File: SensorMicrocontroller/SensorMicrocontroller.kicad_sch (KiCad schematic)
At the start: 35 parts, among them J1 JST B6B-PH-SM4-TB, J10 12V Connector, J11 Light Connector, J2 JST B4B-PH-SM4-TB, J3 JST B4B-PH-SM4-TB, J4 JST B4B-PH-SM4-TB, J5 JST B4B-PH-SM4-TB, J6 Fan0, J7 Fan1, J8 Fan2, J9 Fan3, Q1 DMT6009LCT, Q2 DMT6009LCT, U1 SC0915, U2 ADS1115IDGS

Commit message: Added manufacturer part number to parts
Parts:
- C1: Manufacturer Part Number (none) -> CC0805KRX7R9BB104
- F1: Manufacturer Part Number (none) -> MFU0805FF01000P500
- J1: Manufacturer Part Number (none) -> B6B-PH-SM4-TB
- J10: Manufacturer Part Number (none) -> B2B-PH-SM4-TB
- J11: Manufacturer Part Number (none) -> B4B-EH-A
- J2, J3, J4, J5: Manufacturer Part Number (none) -> B4B-PH-SM4-TB
- J6: value Fan0 -> ~; Manufacturer Part Number (none) -> 0470531000
- J7: value Fan1 -> ~; Manufacturer Part Number (none) -> 0470531000
- J8: value Fan2 -> ~; Manufacturer Part Number (none) -> 0470531000
- J9: value Fan3 -> ~; Manufacturer Part Number (none) -> 0470531000
- Q1, Q2: Manufacturer Part Number (none) -> DMT6009LCT
- R1, R2: Manufacturer Part Number (none) -> CRCW08054K70FKEAC
- R10, R11, R12, R7, R8, R9: value 175 -> 174; Manufacturer Part Number (none) -> RC0805FR-07174RL
- R3, R4, R5, R6: Manufacturer Part Number (none) -> RR1220P-103-D
- U1: value SC0915 -> Pico; Manufacturer Part Number (none) -> SC0915
- U2: Manufacturer Part Number (none) -> ADS1115IDGSR
- U4, U5, U6, U7, U8, U9: value ~ -> Optoisolators; Manufacturer Part Number (none) -> TLP2355(TPL,E
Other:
- note added: "Fan0"
- note added: "Fan1"
- note added: "Fan2"
- note added: "Fan3"

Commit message: Updated date and revision number
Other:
- note added: "1.4"
- note added: "1/27/25"
- note removed: "1.3"
- note removed: "1/9/25"

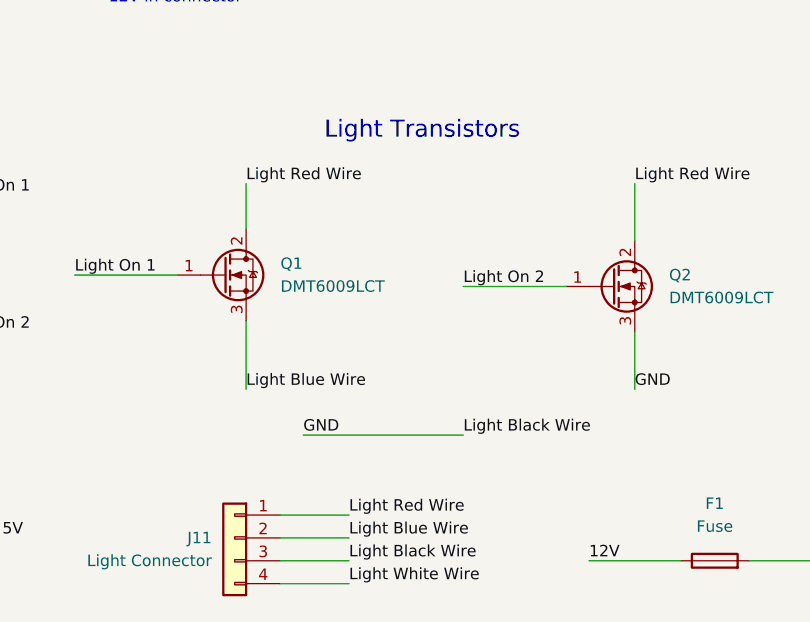
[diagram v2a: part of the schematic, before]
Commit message: Updated transistor wiring diagram
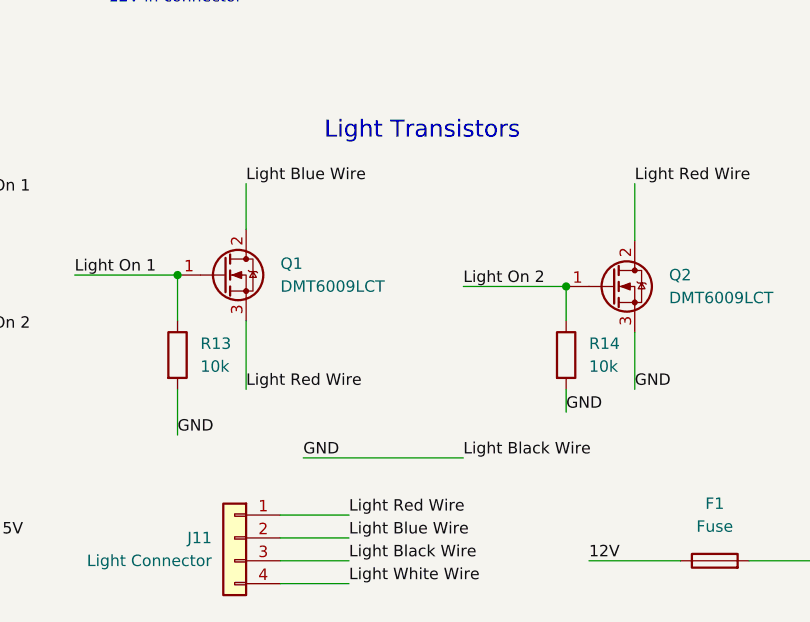
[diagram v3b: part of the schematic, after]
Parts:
- added R13, R14: 10k, Resistor_SMD:R_0805_2012Metric, symbol Device:R
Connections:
- net GND: now also R13.2, R14.2
- net Light Blue Wire: now also Q1.2 (D); no longer Q1.3 (S)
- net Light On 1: now also R13.1
- net Light On 2: now also R14.1
- net Light Red Wire: now also Q1.3 (S); no longer Q1.2 (D)

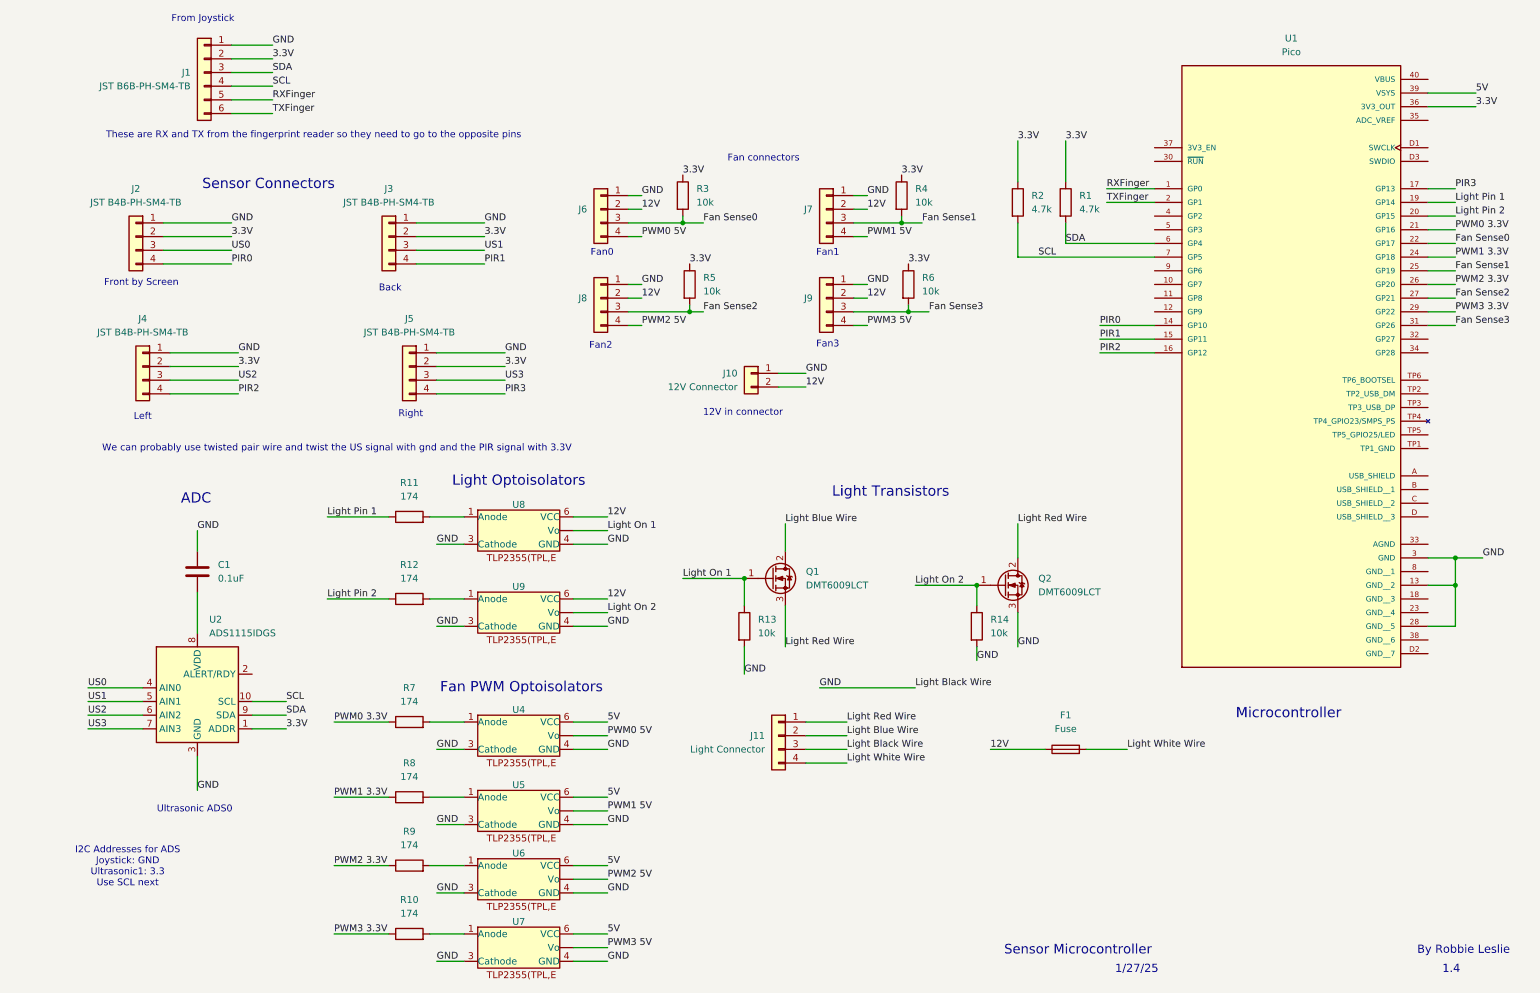
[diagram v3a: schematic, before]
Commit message: Worked on PCB layout
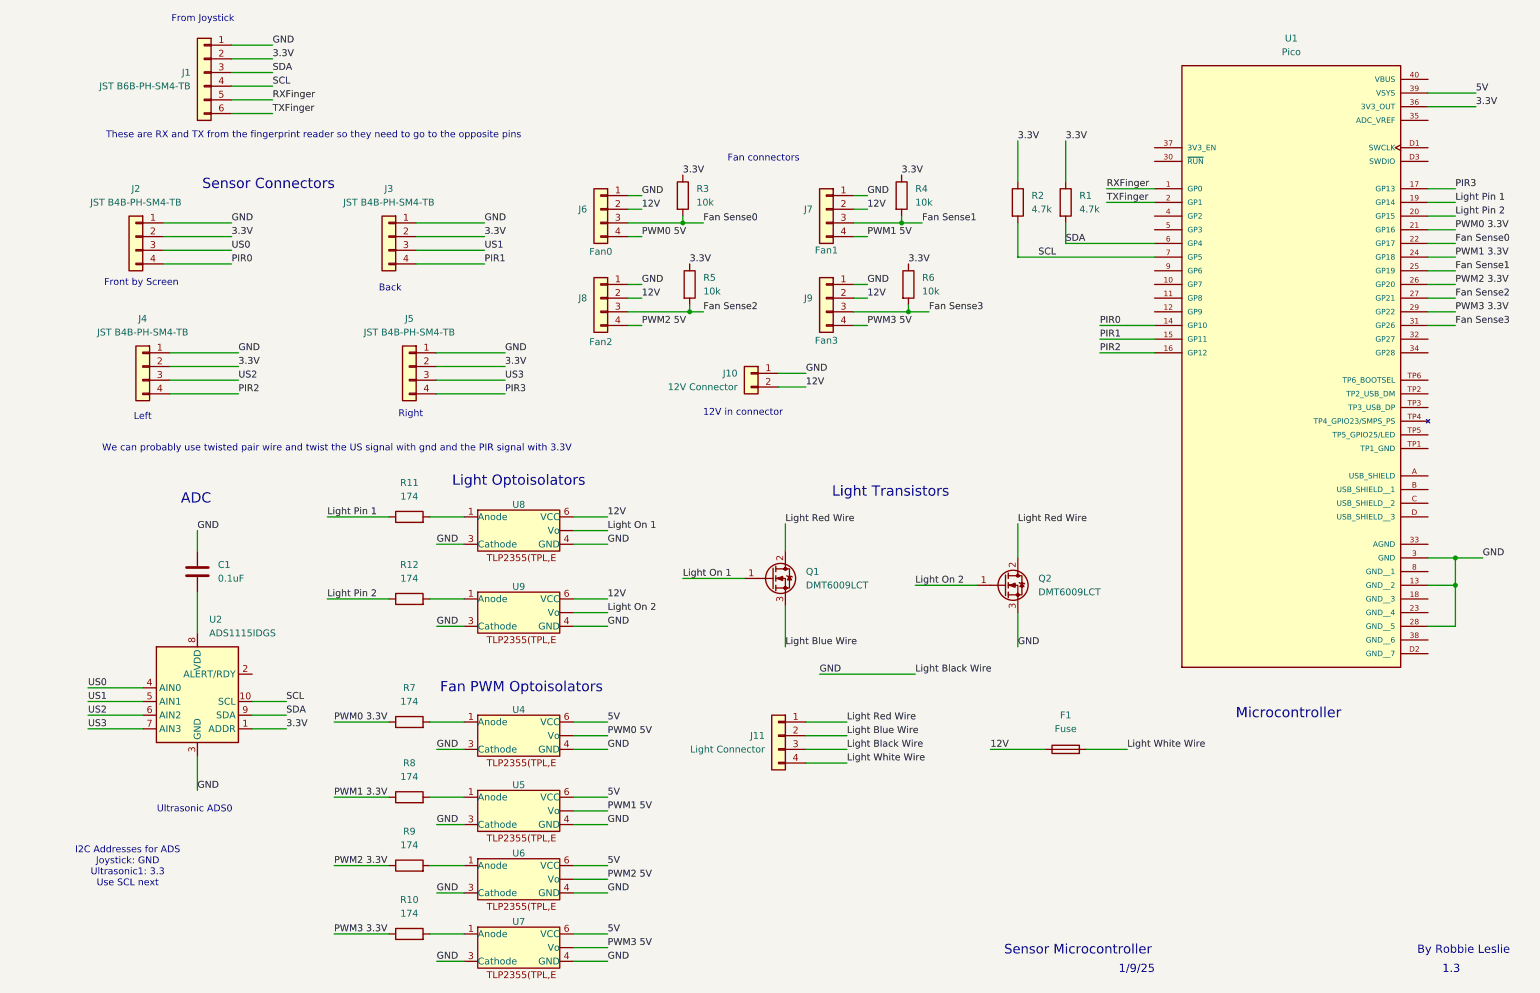
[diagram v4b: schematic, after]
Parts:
- removed R13, R14: 10k, Resistor_SMD:R_0805_2012Metric, symbol Device:R
- J1: Header Connection (none) -> Joystick
- J10: Header Connection (none) -> 12V
- J11: Header Connector (none) -> Light
- J2: Header Connection (none) -> Front Screen
- J3: Header Connection (none) -> Back
- J4: Header Connection (none) -> Left
- J5: Header Connection (none) -> Right
- J6: Fan Number (none) -> Fan0
- J7: Fan Number (none) -> Fan1
- J8: Fan Number (none) -> Fan2
- J9: Fan Number (none) -> Fan3
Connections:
- net Light Blue Wire: now also Q1.3 (S); no longer Q1.2 (D)
- net Light Red Wire: now also Q1.2 (D); no longer Q1.3 (S)
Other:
- note added: "1.3"
- note added: "1/9/25"
- note removed: "1.4"
- note removed: "1/27/25"
- note removed: "Fan0"
- note removed: "Fan1"
- note removed: "Fan2"
- note removed: "Fan3"

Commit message: Finished PCB layout and started routing
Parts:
- added H1, H2, H3, H4: MountingHole, MountingHole:MountingHole_3.2mm_M3_DIN965_Pad, symbol Mechanical:MountingHole
- Q1, Q2: footprint Package_TO_SOT_THT:TO-220-3_Horizontal_TabUp -> Package_TO_SOT_THT:TO-220-3_Vertical
- renumbered J2 to J1, J7 to J10, J9 to J11, J4 to J2, J1 to J3, J3 to J4, J8 to J7, J10 to J8, J11 to J9, R11 to R1, R6 to R10, R2 to R11, R1 to R12, R12 to R2, R7 to R3, R8 to R4, R9 to R5, R10 to R6, R3 to R7, R5 to R8, R4 to R9, U2 to U1, U8 to U2, U9 to U3, U1 to U8
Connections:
- net Light On 1: now also U2.5 (Vo); no longer U2. (Vo)
- net Light On 2: now also U3.5 (Vo); no longer U3. (Vo)
- net PWM0 5V: now also U4.5 (Vo); no longer U4. (Vo)
- net PWM1 5V: now also U5.5 (Vo); no longer U5. (Vo)
- net PWM2 5V: now also U6.5 (Vo); no longer U6. (Vo)
- net PWM3 5V: now also U7.5 (Vo); no longer U7. (Vo)
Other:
- note added: "1/28/25"
- note removed: "1/9/25"

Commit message: Initial version of PCB
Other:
- note added: "1.0"
- note removed: "1.3"

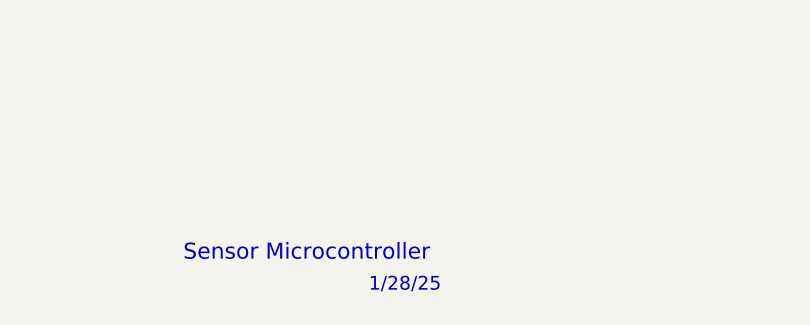
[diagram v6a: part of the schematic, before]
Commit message: Swapped M3 screws to ISO 7380
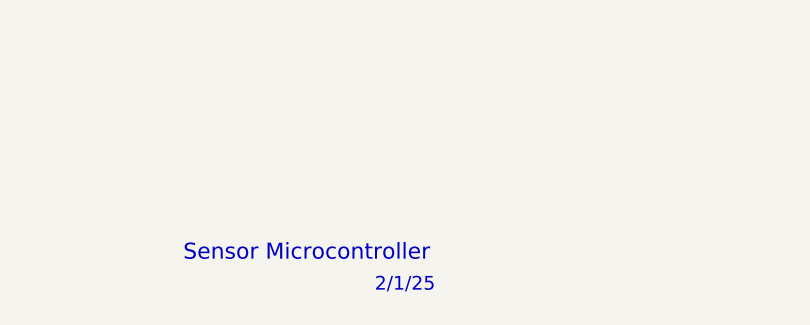
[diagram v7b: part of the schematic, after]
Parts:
- H1, H2, H3, H4: footprint MountingHole:MountingHole_3.2mm_M3_DIN965_Pad -> MountingHole:MountingHole_3.2mm_M3_ISO7380_Pad
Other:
- note added: "2/1/25"
- note removed: "1/28/25"

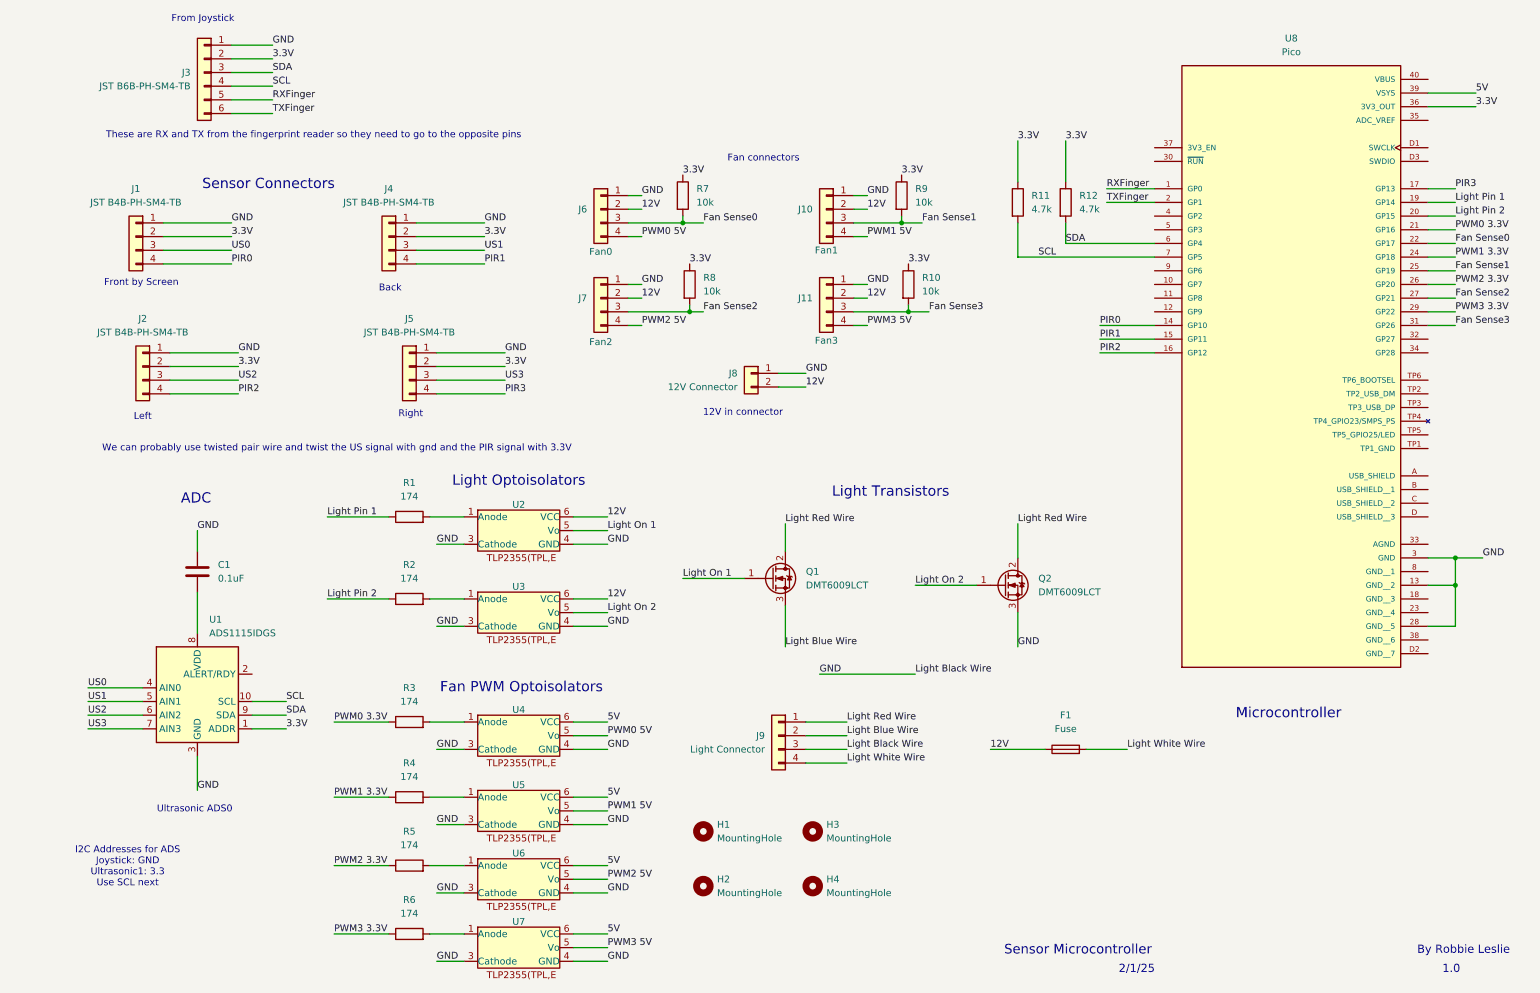
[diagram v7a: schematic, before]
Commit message: Added caps for photocouplers
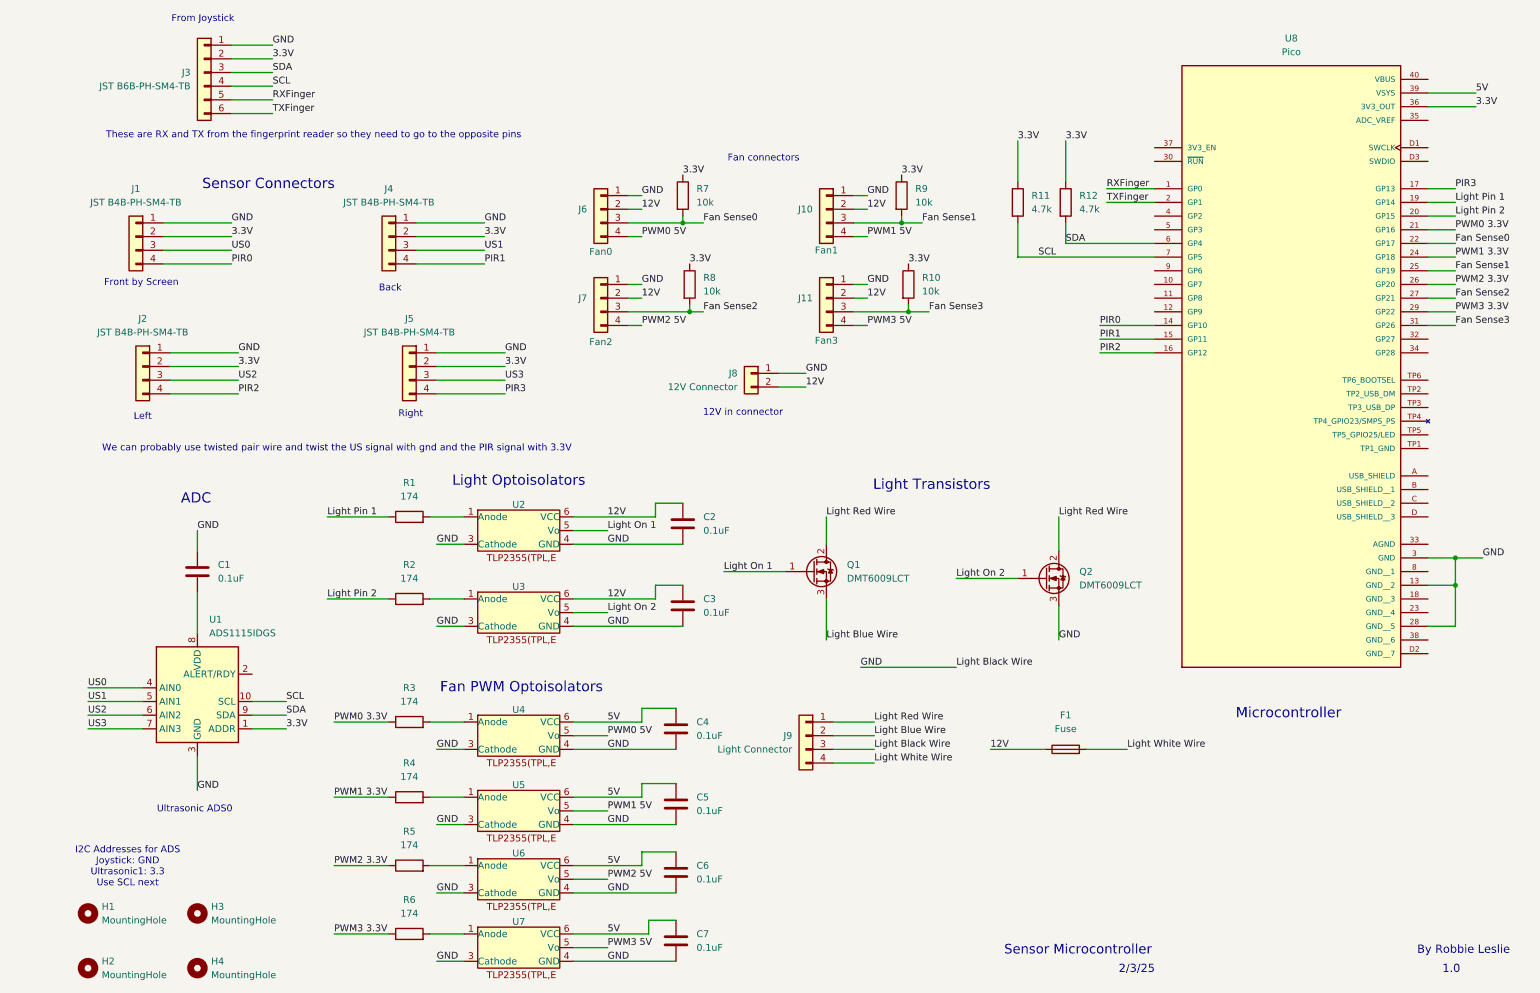
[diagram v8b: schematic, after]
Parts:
- added C2, C3, C4, C5, C6, C7: 0.1uF, Capacitor_SMD:C_0805_2012Metric, symbol Device:C
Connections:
- net 12V: now also C2.1, C3.1
- net 5V: now also C4.1, C5.1, C6.1, C7.1
- net GND: now also C2.2, C3.2, C4.2, C5.2, C6.2, C7.2
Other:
- note added: "2/3/25"
- note removed: "2/1/25"
- moved on the sheet: H1, H2, H3, H4, J9, Q1, Q2
